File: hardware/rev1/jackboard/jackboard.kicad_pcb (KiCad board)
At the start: 2 copper layers, 40 x 108 mm, 13 parts, among them J1 AudioJack2_SwitchT, J10 AudioJack2_SwitchT, J11 USB_B, J2 Conn_01x10_Female, J3 Conn_01x10_Female, J4 AudioJack2_SwitchT, J5 AudioJack2_SwitchT, J6 AudioJack2_SwitchT, J7 AudioJack2_SwitchT, J8 AudioJack2_SwitchT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

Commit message: Wrap up prototype jackboard
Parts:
- added REF**: MountingHole_3.2mm_M3, MountingHole:MountingHole_3.2mm_M3, F.Cu at (125.0, 61.0)
- added REF**: MountingHole_3.2mm_M3, MountingHole:MountingHole_3.2mm_M3, F.Cu at (149.0, 61.0)
- added SW1: SW_Push, Button_Switch_THT:SW_PUSH_6mm, F.Cu at (121.0, 82.0)
- moved J7 5.00 mm to (146.2, 129.1)
- moved J8 5.00 mm to (128.4, 129.1)
- moved J1 5.00 mm to (146.2, 94.4)
- moved J10 5.00 mm to (128.4, 146.4)
- moved J4 5.00 mm to (128.4, 94.4)
- moved J5 5.00 mm to (146.2, 111.7)
- moved J6 5.00 mm to (128.4, 111.7)
- moved J9 5.00 mm to (146.2, 146.4)
- moved D1 3.87 mm to (135.1, 78.0)
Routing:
- net Reset: track 0.00 -> 46.7 mm
- net GATE_D_OUT: track 0.00 -> 43.0 mm
- net GATE_A_OUT: track 0.00 -> 34.1 mm
- net GATE_C_OUT: track 0.00 -> 20.9 mm
- net GATE_B_OUT: track 0.00 -> 9.27 mm
- net CV_A: track 28.8 -> 20.1 mm
- net +3V3: track 47.3 -> 40.4 mm
- net CV_C: track 12.3 -> 18.3 mm
- net CV_D: track 27.0 -> 32.7 mm
- net NEOPIXEL: track 37.1 -> 32.9 mm
- net CV_B: track 10.7 -> 8.61 mm
- net GND: vias 0 -> 18
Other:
- board text added: "Sol Jackpanel"
- board text added: "Winterbloom CC BY-SA 4.0 v3 2020/3/2 wntr.dev/sol"
- board text removed: "Alethea Flowers CC-BY-SA 4.0 v1 2020/1/15 wntr.dev"
- board text removed: "Winterbloom Sol Jackpanel"

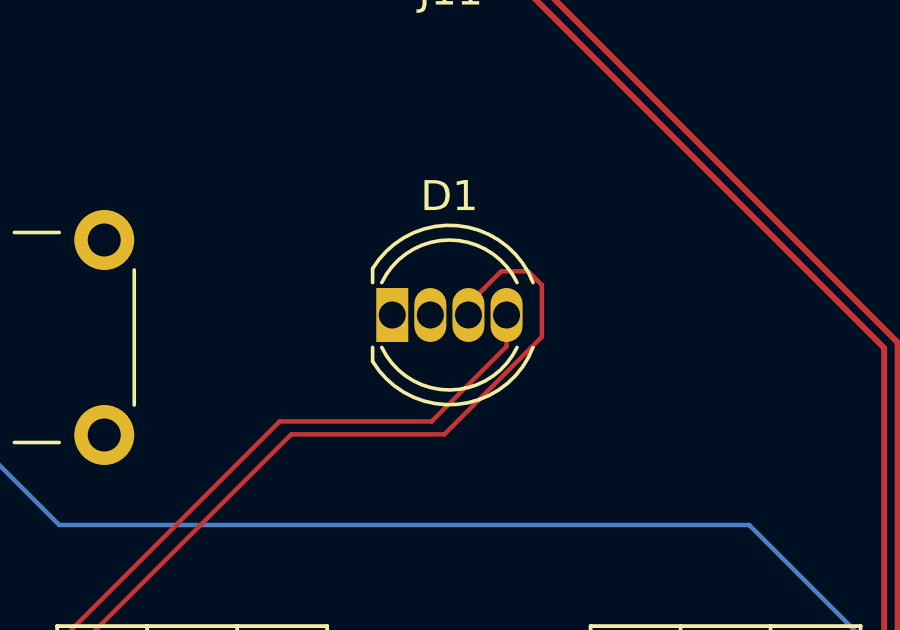
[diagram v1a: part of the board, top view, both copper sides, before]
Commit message: Add blank panel
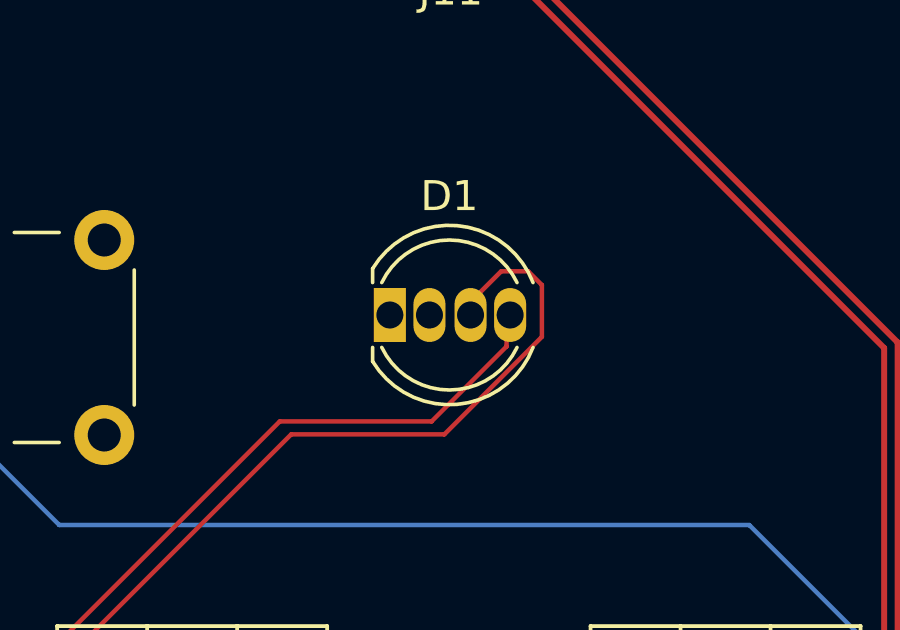
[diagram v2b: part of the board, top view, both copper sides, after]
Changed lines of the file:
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@@
     (visible_elements 7FFFFFFF)
     (pcbplotparams
-      (layerselection 0x010fc_ffffffff)
+      (layerselection 0x010e0_ffffffff)
       (usegerberextensions false)
       (usegerberattributes false)
@@
     (add_net SWCLK)
     (add_net SWDIO)
+  )
+  (module LED_THT:LED_D5.0mm-4_RGB (layer F.Cu)
+    (at 135.1 78)
+    (descr "LED, diameter 5.0mm, 2 pins, diameter 5.0mm, 3 pins, diameter 5.0mm, 4 pins, http://www.kingbright.com/attachments/file/psearch/000/00/00/L-154A4SUREQBFZGEW(Ver.9A).pdf")
+    (tags "LED diameter 5.0mm 2 pins diameter 5.0mm 3 pins diameter 5.0mm 4 pins RGB RGBLED")
+    (fp_text reference D1 (at 1.905 -3.96) (layer F.SilkS)
+      (effects (font (size 1 1) (thickness 0.15)))
+    )
+    (fp_text value NeoPixel_THT (at 1.905 3.96) (layer F.Fab)
+      (effects (font (size 1 1) (thickness 0.15)))
+    )
+    (fp_arc (start 1.905 0) (end -0.595 -1.469694) (angle 299.1) (layer F.Fab) (width 0.1))
+    (fp_arc (start 1.905 0) (end -0.655 -1.54483) (angle 127.7) (layer F.SilkS) (width 0.12))
+    (fp_arc (start 1.905 0) (end -0.655 1.54483) (angle -127.7) (layer F.SilkS) (width 0.12))
+    (fp_arc (start 1.905 0) (end -0.349684 -1.08) (angle 128.8) (layer F.SilkS) (width 0.12))
+    (fp_arc (start 1.905 0) (end -0.349684 1.08) (angle -128.8) (layer F.SilkS) (width 0.12))
+    (fp_circle (center 1.905 0) (end 4.405 0) (layer F.Fab) (width 0.1))
+    (fp_line (start -0.595 -1.469694) (end -0.595 1.469694) (layer F.Fab) (width 0.1))
+    (fp_line (start -0.655 -1.545) (end -0.655 -1.08) (layer F.SilkS) (width 0.12))
+    (fp_line (start -0.655 1.08) (end -0.655 1.545) (layer F.SilkS) (width 0.12))
+    (fp_line (start -1.35 -3.25) (end -1.35 3.25) (layer F.CrtYd) (width 0.05))
+    (fp_line (start -1.35 3.25) (end 5.15 3.25) (layer F.CrtYd) (width 0.05))
+    (fp_line (start 5.15 3.25) (end 5.15 -3.25) (layer F.CrtYd) (width 0.05))
+    (fp_line (start 5.15 -3.25) (end -1.35 -3.25) (layer F.CrtYd) (width 0.05))
+    (fp_text user %R (at 1.905 -3.96) (layer F.Fab)
+      (effects (font (size 1 1) (thickness 0.15)))
+    )
+    (pad 1 thru_hole rect (at -0.08 0) (size 1.07 1.8) (drill 0.9) (layers *.Cu *.Mask)
+      (net 17 "Net-(D1-Pad1)"))
+    (pad 2 thru_hole oval (at 1.24 0) (size 1.07 1.8) (drill 0.9) (layers *.Cu *.Mask)
+      (net 1 GND))
+    (pad 3 thru_hole oval (at 2.61 0) (size 1.07 1.8) (drill 0.9) (layers *.Cu *.Mask)
+      (net 16 +3V3))
+    (pad 4 thru_hole oval (at 3.93 0) (size 1.07 1.8) (drill 0.9) (layers *.Cu *.Mask)
+      (net 3 NEOPIXEL))
+    (model ${KISYS3DMOD}/LED_THT.3dshapes/LED_D5.0mm-4_RGB.wrl
+      (at (xyz 0 0 0))
+      (scale (xyz 1 1 1))
+      (rotate (xyz 0 0 0))
+    )
   )
   (module MountingHole:MountingHole_3.2mm_M3 (layer F.Cu)
@@
       (net 1 GND) (solder_mask_margin 0.1016))
   )
-  (module LED_THT:LED_D5.0mm-4_RGB (layer F.Cu)
-    (at 135.1 78)
-    (descr "LED, diameter 5.0mm, 2 pins, diameter 5.0mm, 3 pins, diameter 5.0mm, 4 pins, http://www.kingbright.com/attachments/file/psearch/000/00/00/L-154A4SUREQBFZGEW(Ver.9A).pdf")
-    (tags "LED diameter 5.0mm 2 pins diameter 5.0mm 3 pins diameter 5.0mm 4 pins RGB RGBLED")
-    (fp_text reference D1 (at 1.905 -3.96) (layer F.SilkS)
-      (effects (font (size 1 1) (thickness 0.15)))
-    )
-    (fp_text value NeoPixel_THT (at 1.905 3.96) (layer F.Fab)
-      (effects (font (size 1 1) (thickness 0.15)))
-    )
-    (fp_arc (start 1.905 0) (end -0.595 -1.469694) (angle 299.1) (layer F.Fab) (width 0.1))
-    (fp_arc (start 1.905 0) (end -0.655 -1.54483) (angle 127.7) (layer F.SilkS) (width 0.12))
-    (fp_arc (start 1.905 0) (end -0.655 1.54483) (angle -127.7) (layer F.SilkS) (width 0.12))
-    (fp_arc (start 1.905 0) (end -0.349684 -1.08) (angle 128.8) (layer F.SilkS) (width 0.12))
-    (fp_arc (start 1.905 0) (end -0.349684 1.08) (angle -128.8) (layer F.SilkS) (width 0.12))
-    (fp_circle (center 1.905 0) (end 4.405 0) (layer F.Fab) (width 0.1))
-    (fp_line (start -0.595 -1.469694) (end -0.595 1.469694) (layer F.Fab) (width 0.1))
-    (fp_line (start -0.655 -1.545) (end -0.655 -1.08) (layer F.SilkS) (width 0.12))
-    (fp_line (start -0.655 1.08) (end -0.655 1.545) (layer F.SilkS) (width 0.12))
-    (fp_line (start -1.35 -3.25) (end -1.35 3.25) (layer F.CrtYd) (width 0.05))
-    (fp_line (start -1.35 3.25) (end 5.15 3.25) (layer F.CrtYd) (width 0.05))
-    (fp_line (start 5.15 3.25) (end 5.15 -3.25) (layer F.CrtYd) (width 0.05))
-    (fp_line (start 5.15 -3.25) (end -1.35 -3.25) (layer F.CrtYd) (width 0.05))
-    (fp_text user %R (at 1.905 -3.96) (layer F.Fab)
-      (effects (font (size 1 1) (thickness 0.15)))
-    )
-    (pad 1 thru_hole rect (at 0 0) (size 1.07 1.8) (drill 0.9) (layers *.Cu *.Mask)
-      (net 17 "Net-(D1-Pad1)"))
-    (pad 2 thru_hole oval (at 1.27 0) (size 1.07 1.8) (drill 0.9) (layers *.Cu *.Mask)
-      (net 1 GND))
-    (pad 3 thru_hole oval (at 2.54 0) (size 1.07 1.8) (drill 0.9) (layers *.Cu *.Mask)
-      (net 16 +3V3))
-    (pad 4 thru_hole oval (at 3.81 0) (size 1.07 1.8) (drill 0.9) (layers *.Cu *.Mask)
-      (net 3 NEOPIXEL))
-    (model ${KISYS3DMOD}/LED_THT.3dshapes/LED_D5.0mm-4_RGB.wrl
-      (at (xyz 0 0 0))
-      (scale (xyz 1 1 1))
-      (rotate (xyz 0 0 0))
-    )
-  )
   (module Button_Switch_THT:SW_PUSH_6mm (layer F.Cu)
